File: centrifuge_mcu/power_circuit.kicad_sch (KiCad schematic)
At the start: 60 parts, among them U2 TPS54294

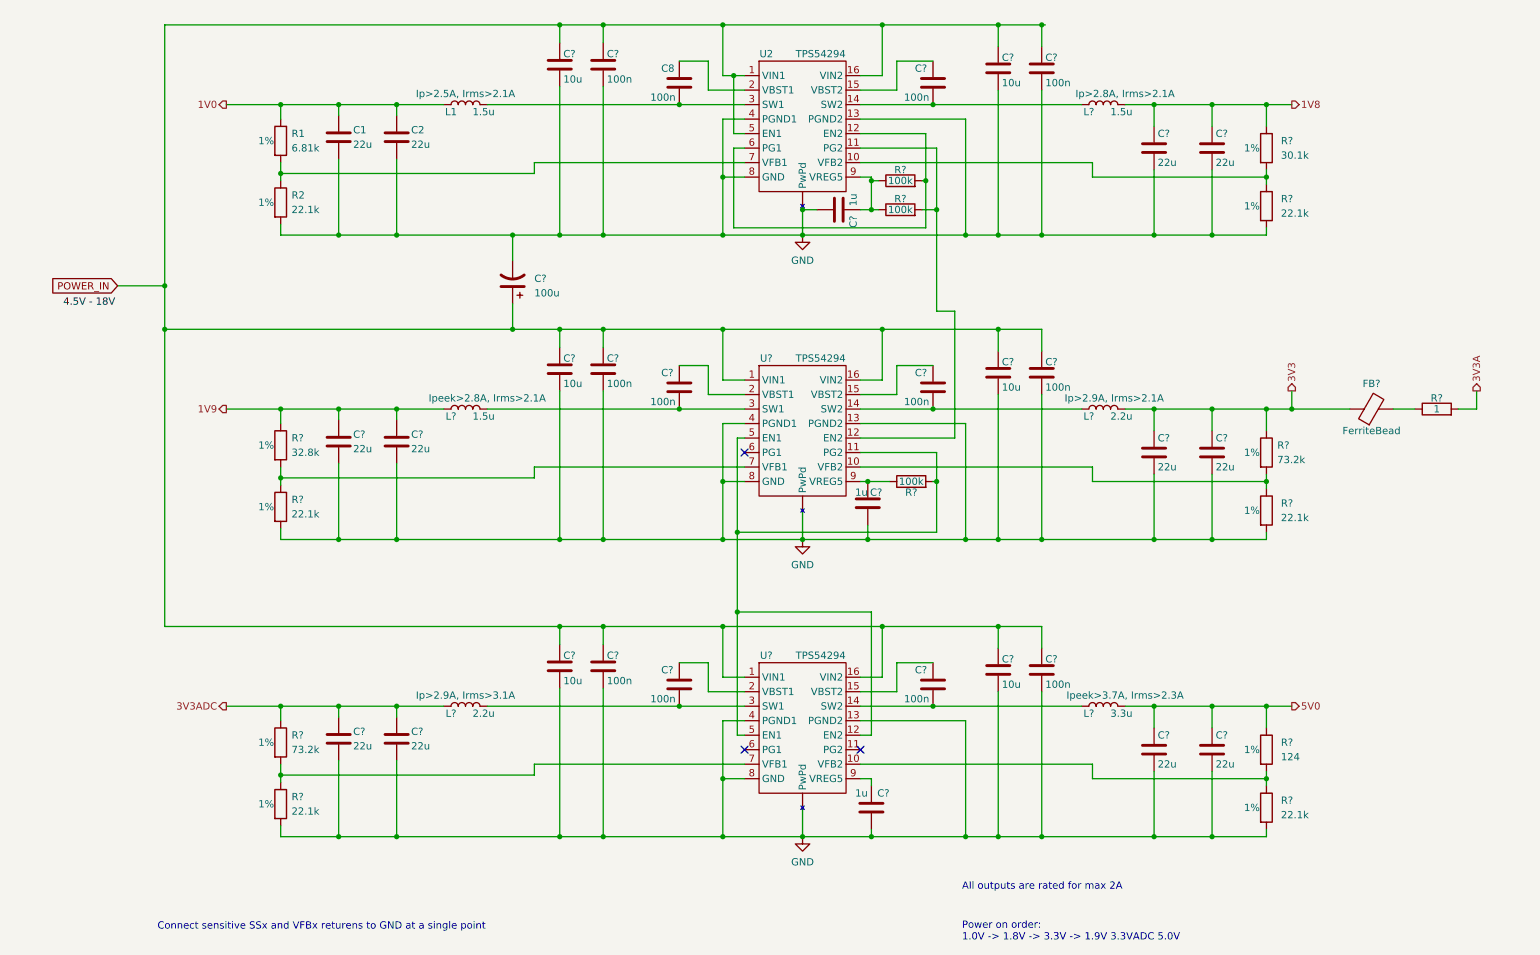
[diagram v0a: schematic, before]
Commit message: make and pick footprints for almost everything
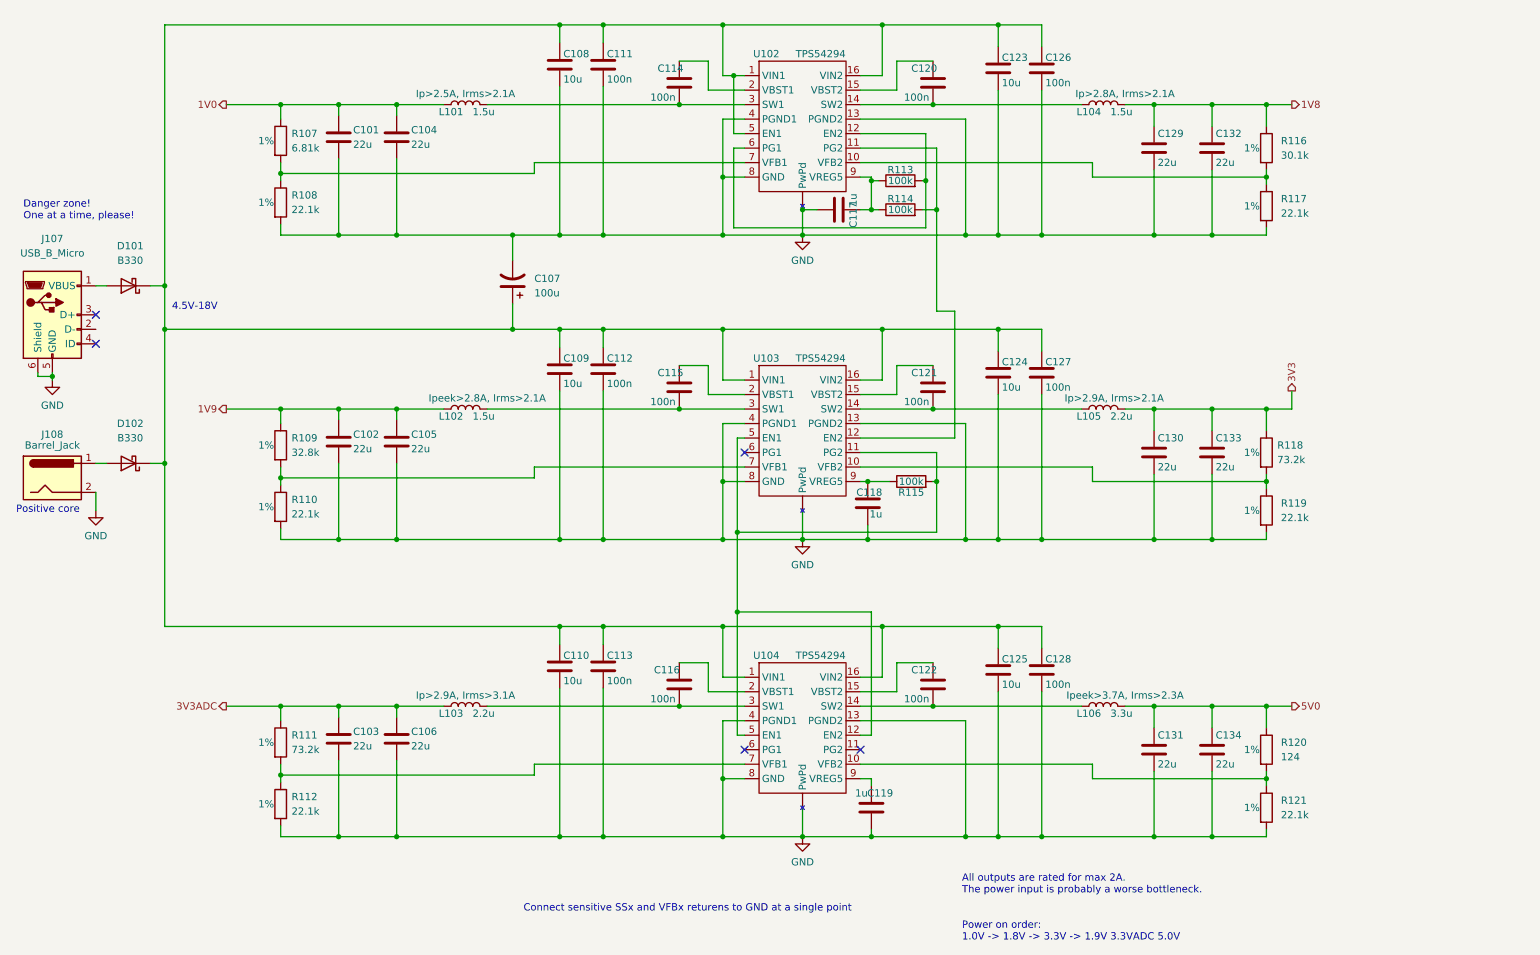
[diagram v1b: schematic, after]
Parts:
- removed FB?: FerriteBead, symbol Device:FerriteBead
- removed R?: 1, symbol Device:R
- added D101, D102: B330, centrifuge_mcu:SMA (DO-214AC), symbol Diode:B330
- added J107: USB_B_Micro, Connector_USB:USB_Micro-B_Molex-105017-0001, symbol Connector:USB_B_Micro
- added J108: Barrel_Jack, Connector_BarrelJack:BarrelJack_CUI_PJ-102AH_Horizontal, symbol Connector:Barrel_Jack
- C101: renamed from C1; footprint (none) -> Capacitor_SMD:C_1206_3216Metric_Pad1.33x1.80mm_HandSolder; Purchase (none) -> https://www.digikey.no/no/products/detail/samsung-electro-m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
- C102, C103, C105, C106, C129, C130, C131, C132, C133, C134: renamed from C?; footprint (none) -> Capacitor_SMD:C_1206_3216Metric_Pad1.33x1.80mm_HandSolder; Purchase (none) -> https://www.digikey.no/no/products/detail/samsung-electro-m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
- C104: renamed from C2; footprint (none) -> Capacitor_SMD:C_1206_3216Metric_Pad1.33x1.80mm_HandSolder; Purchase (none) -> https://www.digikey.no/no/products/detail/samsung-electro-m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
- C107: renamed from C?; footprint (none) -> Capacitor_THT:CP_Radial_D10.0mm_P5.00mm; Purchase (none) -> https://www.digikey.no/no/products/detail/panasonic-electro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
- C108, C109, C110, C123, C124, C125: renamed from C?; footprint (none) -> Capacitor_SMD:C_1206_3216Metric_Pad1.33x1.80mm_HandSolder; Purchase (none) -> https://www.digikey.no/no/products/detail/murata-electronic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
- C111, C112, C113, C115, C116, C120, C121, C122, C126, C127, C128: renamed from C?; footprint (none) -> Capacitor_SMD:C_1206_3216Metric_Pad1.33x1.80mm_HandSolder; Purchase (none) -> https://www.digikey.no/no/products/detail/walsin-technology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
- C114: renamed from C8; footprint (none) -> Capacitor_SMD:C_1206_3216Metric_Pad1.33x1.80mm_HandSolder; Purchase (none) -> https://www.digikey.no/no/products/detail/walsin-technology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
- C117, C118, C119: renamed from C?; footprint (none) -> Capacitor_SMD:C_0805_2012Metric_Pad1.18x1.45mm_HandSolder; Purchase (none) -> https://www.digikey.no/no/products/detail/kemet/C0805C105J4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
- L101: renamed from L1; footprint (none) -> centrifuge_mcu:L_Sumida_CR75; Purchase (none) -> https://www.digikey.no/no/products/detail/sumida-america-in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
- L102, L104: renamed from L?; footprint (none) -> centrifuge_mcu:L_Sumida_CR75; Purchase (none) -> https://www.digikey.no/no/products/detail/sumida-america-in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
- gave numbers to parts that had none: 18
- renumbered R1 to R107, R2 to R108, U2 to U102
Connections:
- net GND: now also J107.5 (GND), J107.6 (Shield), J108.2
- net POWER_IN: no longer names the net of C107.1, C108.1, C109.1, C110.1, C111.1, C112.1, C113.1, C123.1, C124.1, C125.1, C126.1, C127.1, C128.1, U102.1 (VIN1), U102.16 (VIN2), U102.5 (EN1), U103.1 (VIN1), U103.16 (VIN2), U104.1 (VIN1), U104.16 (VIN2)
- net POWER_IN: now also D101.1 (K), D102.1 (K)
- new net: D101.2 (A), J107.1 (VBUS)
- new net: D102.2 (A), J108.1
- no-connect marks 3 -> 5
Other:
- note added: "4.5V-18V"
- note added: "All outputs are rated for max 2A. The power input is probably a worse bottleneck."
- note added: "Danger zone! One at a time, please!"
- note added: "Positive core"
- note removed: "All outputs are rated for max 2A"

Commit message: more footprints, add links to resistor and inductance purchase
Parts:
- removed D101, D102: B330, centrifuge_mcu:SMA (DO-214AC), symbol Diode:B330
- added Q101: Q_PMOS_DGS, Package_TO_SOT_THT:TO-220-3_Vertical, symbol Device:Q_PMOS_GDS
- added R108: 5.49M, Resistor_SMD:R_0805_2012Metric_Pad1.20x1.40mm_HandSolder, symbol Device:R
- J109: renamed from J108; symbol Connector:Barrel_Jack -> Connector:Barrel_Jack_Switch
- L103: footprint (none) -> Inductor_SMD:L_Vishay_IHLP-2020; Purchase (none) -> https://www.digikey.no/no/products/detail/vishay-dale/IHLP2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; Tolerance Ip>2.9A, Irms>3.1A -> Ip>2.9A, Irms>2.1A
- L105: footprint (none) -> Inductor_SMD:L_Vishay_IHLP-2020; Purchase (none) -> https://www.digikey.no/no/products/detail/vishay-dale/IHLP2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
- L106: footprint (none) -> centrifuge_mcu:L_TDK_7065; Purchase (none) -> https://www.digikey.no/no/products/detail/tdk-corporation/S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
- R109: renamed from R107; footprint (none) -> Resistor_SMD:R_0805_2012Metric_Pad1.20x1.40mm_HandSolder; Purchase (none) -> https://www.digikey.no/no/products/detail/stackpole-electro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
- R110: renamed from R108; footprint (none) -> Resistor_SMD:R_0805_2012Metric_Pad1.20x1.40mm_HandSolder; Purchase (none) -> https://www.digikey.no/no/products/detail/stackpole-electro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
- R111: renamed from R109; value 32.8k -> 33k; footprint (none) -> Resistor_SMD:R_0805_2012Metric_Pad1.20x1.40mm_HandSolder; Purchase (none) -> https://www.digikey.no/no/products/detail/yageo/AC0805FR-07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
- R112: renamed from R110; footprint (none) -> Resistor_SMD:R_0805_2012Metric_Pad1.20x1.40mm_HandSolder; Purchase (none) -> https://www.digikey.no/no/products/detail/stackpole-electro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
- R113: renamed from R111; footprint (none) -> Resistor_SMD:R_0805_2012Metric_Pad1.20x1.40mm_HandSolder; Purchase (none) -> https://www.digikey.no/no/products/detail/yageo/RC0805FR-07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
- R114: renamed from R112; footprint (none) -> Resistor_SMD:R_0805_2012Metric_Pad1.20x1.40mm_HandSolder; Purchase (none) -> https://www.digikey.no/no/products/detail/stackpole-electro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
- R115: renamed from R113; footprint (none) -> Resistor_SMD:R_0805_2012Metric_Pad1.20x1.40mm_HandSolder; Purchase (none) -> https://www.digikey.no/no/products/detail/yageo/AC0805FR-07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
- R116: renamed from R114; footprint (none) -> Resistor_SMD:R_0805_2012Metric_Pad1.20x1.40mm_HandSolder; Purchase (none) -> https://www.digikey.no/no/products/detail/yageo/AC0805FR-07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
- R117: renamed from R115; footprint (none) -> Resistor_SMD:R_0805_2012Metric_Pad1.20x1.40mm_HandSolder; Purchase (none) -> https://www.digikey.no/no/products/detail/yageo/AC0805FR-07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
- R118: renamed from R116; footprint (none) -> Resistor_SMD:R_0805_2012Metric_Pad1.20x1.40mm_HandSolder; Purchase (none) -> https://www.digikey.no/no/products/detail/yageo/RC0805FR-07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
- R119: renamed from R117; footprint (none) -> Resistor_SMD:R_0805_2012Metric_Pad1.20x1.40mm_HandSolder; Purchase (none) -> https://www.digikey.no/no/products/detail/stackpole-electro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
- R120: renamed from R118; footprint (none) -> Resistor_SMD:R_0805_2012Metric_Pad1.20x1.40mm_HandSolder; Purchase (none) -> https://www.digikey.no/no/products/detail/yageo/RC0805FR-07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
- R121: renamed from R119; footprint (none) -> Resistor_SMD:R_0805_2012Metric_Pad1.20x1.40mm_HandSolder; Purchase (none) -> https://www.digikey.no/no/products/detail/stackpole-electro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
- R122: renamed from R120; value 124 -> 124k; footprint (none) -> Resistor_SMD:R_0805_2012Metric_Pad1.20x1.40mm_HandSolder; Purchase (none) -> https://www.digikey.no/no/products/detail/stackpole-electro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
- R123: renamed from R121; footprint (none) -> Resistor_SMD:R_0805_2012Metric_Pad1.20x1.40mm_HandSolder; Purchase (none) -> https://www.digikey.no/no/products/detail/stackpole-electro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
- renumbered J107 to J108
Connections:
- net 1V9: now also R108.1
- net GND: now also Q101.1 (G); no longer J108.5 (GND), J108.6 (Shield)
- net at C107.1, C108.1, C109.1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: now also J108.1 (VBUS), Q101.3 (S)
- net at R111.2, R112.1, U103.7 (VFB1): now also R108.2
- net at J109.1: now also Q101.2 (D)
- new net: J108.5 (GND), J108.6 (Shield), J109.3
- no-connect marks 5 -> 6
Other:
- note added: "Reverse polarity protection"
- note added: "USB disconnects when barrel jack attached"
- note removed: "Danger zone! One at a time, please!"
- moved on the sheet: C101, C102, C103, C104, C105, C106, C107, C108, C109, C110, C111, C112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

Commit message: last footprints, time to route (after final FPGA-board connectors)
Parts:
- added J110: PowerIn, Connector_PinHeader_2.54mm:PinHeader_1x02_P2.54mm_Vertical, symbol Connector:Conn_01x02_Male
- added J111: PowerPads, centrifuge_mcu:PowerPads, symbol Connector:Conn_01x02_Male
- R107: renamed from R108; value 5.49M -> 5.6M; Purchase https://www.digikey.no/no/products/detail/vishay-dale/CRCW0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 -> https://www.digikey.no/no/products/detail/stackpole-electro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
- U102, U103, U104: footprint (none) -> centrifuge_mcu:TSSOP-16-1EP_4.4x5mm_P0.65mm_EP3x3mm_ThermalVias_EXTRA
- renumbered R109 to R108, R110 to R109, R111 to R110, R112 to R111, R113 to R112, R114 to R113, R115 to R114, R116 to R115, R117 to R116, R118 to R117, R119 to R118, R120 to R119, R121 to R120, R122 to R121, R123 to R122
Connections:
- net GND: now also U102.17 (PwPd), U103.17 (PwPd), U104.17 (PwPd), J110.2 (Pin_2), J111.2 (Pin_2); no longer U102. (PwPd), U103. (PwPd), U104. (PwPd)
- net at J109.1, Q101.2 (D): now also J110.1 (Pin_1), J111.1 (Pin_1)
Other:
- moved on the sheet: Q101
